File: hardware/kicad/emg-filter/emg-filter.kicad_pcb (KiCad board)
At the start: 4 copper layers, 703 parts, among them J1 Conn_01x02, J10 Conn_01x02, J11 Conn_01x02, J12 Conn_01x02, J13 Conn_01x02, J14 Conn_01x02, J15 Conn_01x02, J16 Conn_01x02, J17 Conn_01x02, J18 Conn_01x02, J19 Conn_01x02, J2 Conn_01x03, J20 Conn_01x02, J21 Conn_01x02, J22 Conn_01x02, J23 Conn_01x02, J24 Conn_01x02, J25 Conn_01x02, J26 Conn_01x02, J27 Conn_01x02, J28 Conn_01x02, J29 Conn_01x02, J3 Conn_02x20_Odd_Even, J30 Conn_01x02, J31 Conn_01x02, J32 Conn_01x02, J33 Conn_01x02, J34 Conn_01x02, J35 Conn_01x02, J36 Conn_01x02, J37 Conn_01x02, J38 Conn_01x02, J39 Conn_01x02, J4 Conn_01x02, J40 Conn_01x02, J41 Conn_01x02, J42 Conn_01x02, J43 Conn_01x02, J44 Conn_01x02, J45 Conn_01x02, J46 Conn_01x02, J47 Conn_01x02, J48 Conn_01x02, J49 Conn_01x02, J5 Conn_01x02, J50 Conn_01x02, J51 Conn_01x02, J6 Conn_01x02, J7 Conn_01x02, J8 Conn_01x02, J9 Conn_01x02, U1 LM7805_TO220, U10 LM4565, U11 LM4565, U12 INA2332, U13 LM4565, U14 LM4565, U15 LM4565, U16 LM4565, U17 LM4565, U18 LM4565, U19 INA2332, U2 LM7905_TO220, U20 LM4565, U21 LM4565, U22 LM4565, U23 LM4565, U24 LM4565, U25 LM4565, U26 INA2332, U27 LM4565, U28 LM4565, U29 LM4565, U3 ADC108S102, U30 LM4565, U31 LM4565, U32 LM4565, U33 INA2332, U34 LM4565, U35 LM4565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

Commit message: all channels complete
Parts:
- removed the C206 at (248.0, -16.8)
- removed the C207 at (248.0, -26.7)
- removed the C208 at (250.1, -16.8)
- removed the C209 at (250.1, -26.7)
- removed the C210 at (260.0, -13.5)
- removed the C211 at (262.0, -23.4)
- removed the C212 at (262.0, -13.5)
- removed the C213 at (260.0, -23.4)
- removed the J3 at (267.5, -41.0)
- removed the U51 at (255.0, -14.6)
- removed the U52 at (255.0, -24.5)
- moved C37 162.9 mm to (238.8, 56.3), turned to 0 degrees
- moved C54 159.4 mm to (243.0, 66.1)
- moved C22 149.9 mm to (244.5, 98.2)
- moved C55 143.6 mm to (247.0, 172.9)
- moved C36 143.1 mm to (240.3, 88.4), turned to 180 degrees
- moved C17 143.0 mm to (242.8, 163.1), turned to 180 degrees
- moved C59 142.0 mm to (245.6, 142.1)
- moved C32 137.0 mm to (241.4, 132.3), turned to 0 degrees
- moved C70 115.0 mm to (-11.9, 152.6)
- moved C71 115.0 mm to (-11.9, 165.3)
- moved C72 115.0 mm to (-3.90, 157.0)
- moved C73 115.0 mm to (-3.90, 161.0)
- moved C74 115.0 mm to (0.41, 157.0)
- moved C77 115.0 mm to (0.41, 161.0)
- moved D1 115.0 mm to (-28.3, 158.3)
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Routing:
- net +5V: track 286.8 -> 390.3 mm, vias 24 -> 56
- net (no net): track 20.1 -> 0.00 mm
- net +3V3: track 0.00 -> 8.57 mm
- net -5V: track 236.3 -> 229.0 mm

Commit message: fixed drc errors
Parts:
- moved C70 100.3 mm to (79.2, 110.5)
- moved C77 100.3 mm to (91.5, 118.9)
- moved C21 100.3 mm to (31.8, 116.4)
- moved C26 100.3 mm to (35.8, 116.4)
- moved C35 100.3 mm to (33.8, 116.4)
- moved C52 100.3 mm to (49.2, 109.4)
- moved C53 100.3 mm to (54.1, 123.4)
- moved C71 100.3 mm to (79.2, 123.2)
- moved C72 100.3 mm to (87.2, 114.9)
- moved C73 100.3 mm to (87.2, 118.9)
- moved C74 100.3 mm to (91.5, 114.9)
- moved C75 100.3 mm to (89.3, 118.9)
- moved C76 100.3 mm to (89.3, 114.9)
- moved D1 100.3 mm to (62.8, 116.3)
- moved D2 100.3 mm to (60.2, 123.2)
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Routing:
- net +5V: track 390.3 -> 391.3 mm

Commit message: saving progress
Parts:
- moved J8 257.5 mm to (124.4, 208.0), turned to 270 degrees
- moved R138 244.9 mm to (57.4, 267.1), turned to 270 degrees
- moved D13 244.3 mm to (60.1, 268.1), turned to 0 degrees
- moved R142 244.3 mm to (52.9, 264.2), turned to 180 degrees
- moved C132 241.9 mm to (67.7, 270.3), turned to 0 degrees
- moved U23 241.9 mm to (62.9, 268.1), turned to 90 degrees
- moved R144 241.0 mm to (51.3, 261.4), turned to 90 degrees
- moved D15 240.7 mm to (60.1, 266.1), turned to 180 degrees
- moved U25 240.3 mm to (53.5, 262.3), turned to 90 degrees
- moved R174 240.1 mm to (57.4, 289.4), turned to 270 degrees
- moved R178 239.6 mm to (52.8, 286.5), turned to 180 degrees
- moved D17 239.5 mm to (60.1, 290.4), turned to 0 degrees
- moved J6 238.4 mm to (124.4, 201.5), turned to 270 degrees
- moved R133 238.1 mm to (67.7, 268.2), turned to 0 degrees
- moved R139 237.0 mm to (58.7, 263.3), turned to 90 degrees
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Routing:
- net -VINB_2: track 0.00 -> 18.9 mm
- net -VINA_1: track 0.00 -> 18.6 mm
- net REFA_1: track 7.19 -> 19.3 mm
- net REFB_2: track 7.21 -> 19.3 mm
- net +VINB_2: track 0.00 -> 9.09 mm
- net +VINA_1: track 0.00 -> 9.07 mm

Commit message: saving progress
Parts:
- removed the J10 at (157.4, -20.0)
- removed the J12 at (157.4, -7.01)
- removed the J14 at (157.4, -13.5)
- removed the J4 at (157.4, -26.5)
- removed the J6 at (157.4, -39.5)
- removed the J8 at (157.4, -33.0)
- moved J43 231.3 mm to (155.1, 174.4), turned to 90 degrees
- moved J45 226.8 mm to (155.1, 180.9), turned to 90 degrees
- moved J40 219.5 mm to (144.1, 167.9), turned to 270 degrees
- moved C15 218.5 mm to (199.1, 40.0)
- moved C201 218.5 mm to (184.8, 52.9)
- moved C8 218.5 mm to (199.0, 49.9)
- moved D36 218.5 mm to (216.0, 50.4)
- moved R303 218.5 mm to (190.7, 54.8)
- moved R306 218.5 mm to (199.1, 42.0)
- moved R307 218.5 mm to (199.0, 51.9)
- moved U57 218.5 mm to (203.7, 48.1)
- moved C198 218.5 mm to (176.9, 45.7)
- moved C211 218.5 mm to (207.6, 52.7)
- moved C212 218.5 mm to (208.4, 36.0)
- moved C30 218.5 mm to (216.6, 45.9)
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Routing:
- net -VINB_6: track 0.00 -> 64.9 mm, vias 0 -> 1
- net -VINB_4: track 0.00 -> 64.9 mm, vias 0 -> 1
- net -VINA_13: track 0.00 -> 64.7 mm, vias 0 -> 1
- net -VINA_11: track 0.00 -> 64.6 mm, vias 0 -> 1
- net REFB_12: track 7.17 -> 57.2 mm, vias 1 -> 2
- net REFA_5: track 7.19 -> 57.2 mm, vias 1 -> 2
- net REFB_14: track 7.18 -> 57.0 mm, vias 1 -> 2
- net REFA_7: track 7.19 -> 57.0 mm, vias 1 -> 2
- net REFA_11: track 7.19 -> 57.0 mm, vias 1 -> 2
- net REFA_3: track 7.19 -> 57.0 mm, vias 1 -> 2
- net REFA_15: track 7.19 -> 57.0 mm, vias 1 -> 2
- net REFA_13: track 7.19 -> 56.8 mm, vias 1 -> 2
- net REFB_4: track 7.17 -> 56.8 mm, vias 1 -> 2
- net REFB_6: track 7.18 -> 56.6 mm, vias 1 -> 2
- net -VINB_2: track 18.9 -> 65.1 mm, vias 0 -> 1
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
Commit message: saving progress
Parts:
- moved J3 312.5 mm to (85.6, 218.9), turned to 90 degrees
- moved J1 211.9 mm to (72.4, 209.4), turned to 180 degrees
- moved C78 205.2 mm to (5.84, 111.7)
- moved C81 205.2 mm to (3.81, 111.7)
- moved C82 205.2 mm to (15.7, 115.0)
- moved C84 205.2 mm to (17.8, 115.0)
- moved U4 205.2 mm to (10.8, 114.0)
- moved C21 203.0 mm to (68.9, 206.7), turned to 90 degrees
- moved C35 199.9 mm to (66.8, 206.7), turned to 90 degrees
- moved J2 198.5 mm to (61.0, 212.0), turned to 180 degrees
- moved C26 196.8 mm to (64.8, 206.7), turned to 90 degrees
- moved R1 193.3 mm to (57.3, 211.9), turned to 90 degrees
- moved C85 189.4 mm to (2.86, 99.6), turned to 90 degrees
- moved C52 188.1 mm to (51.5, 213.7), turned to 180 degrees
- moved C83 187.5 mm to (4.89, 99.6), turned to 90 degrees
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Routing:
- net -VINA_15: track 18.7 -> 65.2 mm, vias 0 -> 1
- net +VINB_14: track 9.07 -> 42.3 mm, vias 0 -> 1

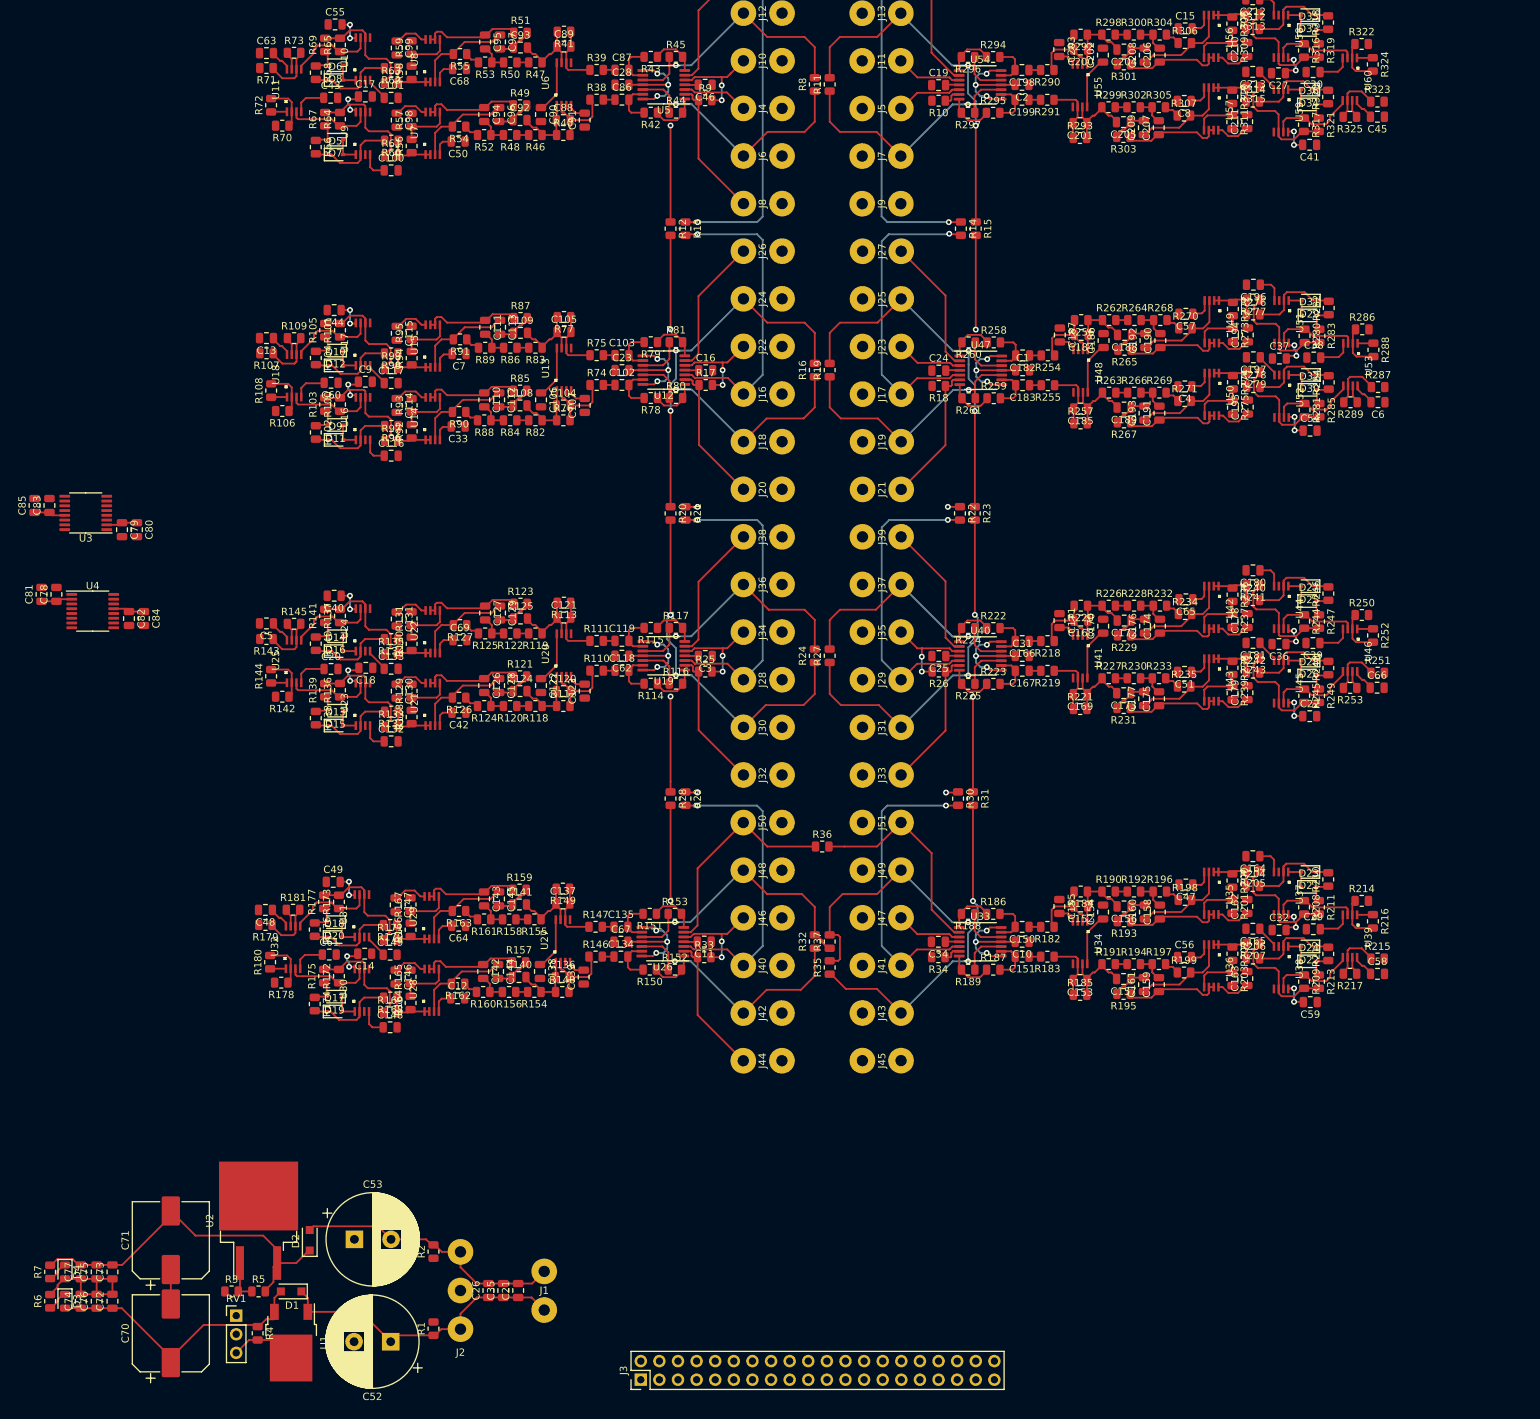
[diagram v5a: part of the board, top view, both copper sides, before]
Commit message: finished adc placement data bus routing
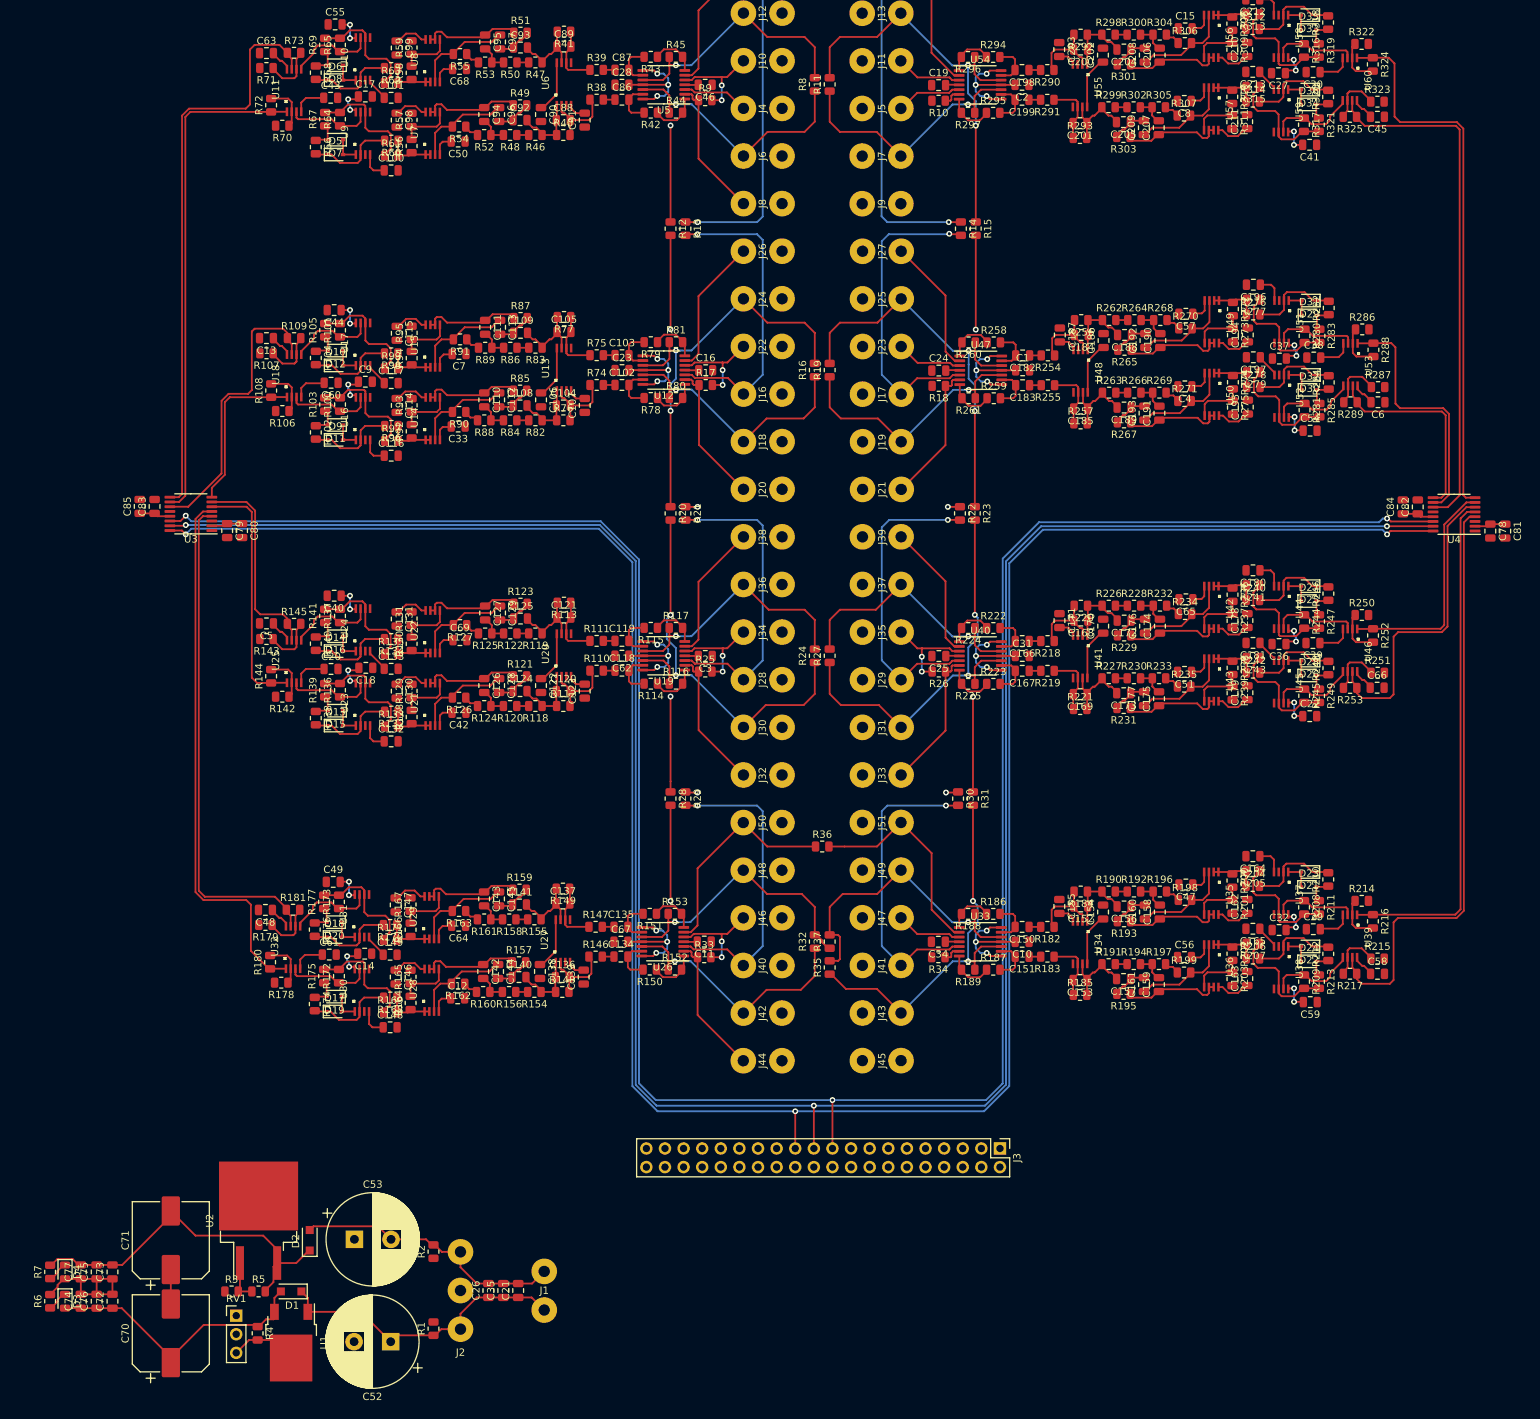
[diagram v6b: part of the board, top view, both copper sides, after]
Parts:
- moved C81 200.0 mm to (203.6, 103.1), turned to 270 degrees
- moved C78 195.9 mm to (201.5, 103.1), turned to 270 degrees
- moved U4 186.3 mm to (196.6, 100.8), turned to 180 degrees
- moved C82 176.6 mm to (191.6, 99.8), turned to 90 degrees
- moved C84 172.5 mm to (189.6, 99.8), turned to 90 degrees
- moved J3 58.3 mm to (134.6, 187.3), turned to 270 degrees
- moved C83 14.4 mm to (19.2, 99.7)
- moved C85 14.4 mm to (17.2, 99.7)
- moved U3 14.4 mm to (24.2, 100.7)
- moved C79 14.4 mm to (29.1, 103.0)
- moved C80 14.4 mm to (31.2, 103.0)
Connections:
- U3 pad 10: OUT_7 -> OUT_1
- U3 pad 11: OUT_8 -> OUT_4
- U3 pad 4: OUT_1 -> OUT_8
- U3 pad 5: OUT_2 -> OUT_7
- U3 pad 6: OUT_3 -> OUT_5
- U3 pad 7: OUT_4 -> OUT_6
- U3 pad 8: OUT_5 -> OUT_3
- U3 pad 9: OUT_6 -> OUT_2
- U4 pad 10: OUT_15 -> OUT_13
- U4 pad 4: OUT_9 -> OUT_10
- U4 pad 5: OUT_10 -> OUT_9
- U4 pad 6: OUT_11 -> OUT_12
- U4 pad 7: OUT_12 -> OUT_11
- U4 pad 8: OUT_13 -> OUT_15
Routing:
- net DIN_MOSI_PI: track 0.00 -> 329.2 mm, vias 0 -> 3
- net SCLK_CLK_PI: track 0.00 -> 328.0 mm, vias 0 -> 3
- net DOUT_MISO_PI: track 0.00 -> 327.6 mm, vias 0 -> 3
- net OUT_10: track 2.49 -> 81.7 mm
- net OUT_2: track 2.49 -> 79.2 mm
- net OUT_15: track 2.17 -> 74.5 mm
- net OUT_7: track 2.17 -> 74.0 mm
- net OUT_16: track 2.49 -> 71.6 mm
- net OUT_9: track 2.17 -> 70.1 mm
- net OUT_1: track 2.17 -> 68.3 mm
- net OUT_8: track 2.49 -> 68.2 mm
- net OUT_12: track 2.49 -> 43.1 mm
- net OUT_4: track 2.49 -> 40.0 mm
- net OUT_13: track 2.17 -> 34.6 mm
- net OUT_5: track 2.17 -> 33.5 mm
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
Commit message: saving progress
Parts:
- moved R6 250.3 mm to (144.2, 0.23), turned to 270 degrees
- moved D3 248.0 mm to (142.2, 0.23), turned to 90 degrees
- moved C74 245.7 mm to (140.1, 0.23), turned to 270 degrees
- moved R7 243.7 mm to (144.2, 4.24), turned to 270 degrees
- moved C76 243.4 mm to (137.9, 0.23), turned to 270 degrees
- moved C70 241.4 mm to (127.8, -4.15), turned to 270 degrees
- moved D4 241.4 mm to (142.2, 4.24), turned to 90 degrees
- moved C72 241.2 mm to (135.7, 0.23), turned to 270 degrees
- moved C77 239.0 mm to (140.1, 4.24), turned to 270 degrees
- moved C75 236.6 mm to (137.9, 4.24), turned to 270 degrees
- moved C73 234.3 mm to (135.7, 4.24), turned to 270 degrees
- moved R4 231.9 mm to (115.9, -4.15), turned to 90 degrees
- moved U1 231.2 mm to (111.3, -5.42), turned to 90 degrees
- moved RV1 229.6 mm to (118.8, -1.73), turned to 180 degrees
- moved R3 224.0 mm to (119.5, 1.57), turned to 180 degrees
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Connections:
- J3 pad 13: !CS_1_PI -> !CS_2_PI
- J3 pad 15: !CS_2_PI -> !CS_1_PI
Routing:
- net !CS_1_PI: track 0.00 -> 169.5 mm, vias 0 -> 1
- net !CS_2_PI: track 0.00 -> 160.2 mm, vias 0 -> 1
- net GNDREF: track 37.6 -> 46.5 mm
- net AGND: track 24.9 -> 33.0 mm
- net +VINA_15: track 9.05 -> 13.7 mm, vias 0 -> 2
- net +VINA_9: track 9.04 -> 13.7 mm, vias 0 -> 2
- net +VINA_13: track 9.07 -> 13.6 mm, vias 0 -> 2

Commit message: saving progress
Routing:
- net +3V3: track 8.57 -> 341.8 mm, vias 0 -> 4
